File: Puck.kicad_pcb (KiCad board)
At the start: 2 copper layers, 26.6 x 72.5 mm, 19 parts, among them J3 TYPE-C-31-M-12, J4 Conn_01x04_Socket, SW1 SW_Push, SW2 SW_Push, U1 ET6226M, U2 ESP32-C6-MINI-1/U, U4 AP2112K-3.3TRG1, U5 MCP9808T-E_MS

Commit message: feat: Disconnect RX and TX pins
Original-author: Ishan Karmakar <ishan.karmakar24@gmail.com>
Source-commit: 296c2ee0a068d96963a51e7bc8ff53979a0f6f0b
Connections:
- J4 pad 1: /RX -> unconnected-(J4-RX-Pad1)
- J4 pad 3: /TX -> unconnected-(J4-TX-Pad3)
- U2 pad 30: /RX -> unconnected-(U2-U0RXD/GPIO17-Pad30)
- U2 pad 31: /TX -> unconnected-(U2-U0TXD/GPIO16-Pad31)
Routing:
- net /RX: track 13.8 -> 0.00 mm, vias 1 -> 0
- net /TX: track 12.8 -> 0.00 mm, vias 1 -> 0
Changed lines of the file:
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@@
 			(size 0.4 0.8)
 			(layers "F.Cu" "F.Mask" "F.Paste")
-			(net "/RX")
+			(net "unconnected-(U2-U0RXD{slash}GPIO17-Pad30)")
 			(pinfunction "U0RXD/GPIO17_30")
-			(pintype "bidirectional")
+			(pintype "bidirectional+no_connect")
 		)
 		(pad "31" smd rect
@@
 			(size 0.4 0.8)
 			(layers "F.Cu" "F.Mask" "F.Paste")
-			(net "/TX")
+			(net "unconnected-(U2-U0TXD{slash}GPIO16-Pad31)")
 			(pinfunction "U0TXD/GPIO16_31")
-			(pintype "bidirectional")
+			(pintype "bidirectional+no_connect")
 		)
 		(pad "32" smd rect
@@
 			(size 0.7874 0.7874)
 			(layers "B.Cu" "B.Mask")
-			(net "/RX")
+			(net "unconnected-(J4-RX-Pad1)")
 			(pinfunction "RX_1")
-			(pintype "bidirectional")
+			(pintype "bidirectional+no_connect")
 		)
 		(pad "2" connect circle
@@
 			(size 0.7874 0.7874)
 			(layers "B.Cu" "B.Mask")
-			(net "/TX")
+			(net "unconnected-(J4-TX-Pad3)")
 			(pinfunction "TX_3")
-			(pintype "bidirectional")
+			(pintype "bidirectional+no_connect")
 		)
 		(pad "4" connect circle
@@
 		(net "/BOOT")
 	)
-	(segment
-		(start 170.2 130)
-		(end 170 129.8)
-		(width 0.2)
-		(layer "F.Cu")
-		(net "/RX")
-	)
-	(segment
-		(start 171.4 119.6)
-		(end 171.4 119)
-		(width 0.2)
-		(layer "F.Cu")
-		(net "/RX")
-	)
-	(segment
-		(start 170 121)
-		(end 171.4 119.6)
-		(width 0.2)
-		(layer "F.Cu")
-		(net "/RX")
-	)
-	(segment
-		(start 170 129.8)
-		(end 170 121)
-		(width 0.2)
-		(layer "F.Cu")
-		(net "/RX")
-	)
-	(via
-		(at 170.2 130)
-		(size 0.6)
-		(drill 0.3)
-		(layers "F.Cu" "B.Cu")
-		(net "/RX")
-	)
-	(segment
-		(start 171.23 130)
-		(end 170.2 130)
-		(width 0.2)
-		(layer "B.Cu")
-		(net "/RX")
-	)
-	(segment
-		(start 172 129.23)
-		(end 171.23 130)
-		(width 0.2)
-		(layer "B.Cu")
-		(net "/RX")
-	)
-	(segment
-		(start 170.6 121)
-		(end 172.2 119.4)
-		(width 0.2)
-		(layer "F.Cu")
-		(net "/TX")
-	)
-	(segment
-		(start 172.2 119.4)
-		(end 172.2 119)
-		(width 0.2)
-		(layer "F.Cu")
-		(net "/TX")
-	)
-	(segment
-		(start 170.6 129.2)
-		(end 170.6 121)
-		(width 0.2)
-		(layer "F.Cu")
-		(net "/TX")
-	)
-	(via
-		(at 170.6 129.2)
-		(size 0.6)
-		(drill 0.3)
-		(layers "F.Cu" "B.Cu")
-		(net "/TX")
-	)
-	(segment
-		(start 171.84 127.96)
-		(end 170.6 129.2)
-		(width 0.2)
-		(layer "B.Cu")
-		(net "/TX")
-	)
-	(segment
-		(start 172 127.96)
-		(end 171.84 127.96)
-		(width 0.2)
-		(layer "B.Cu")
-		(net "/TX")
-	)
 	(zone

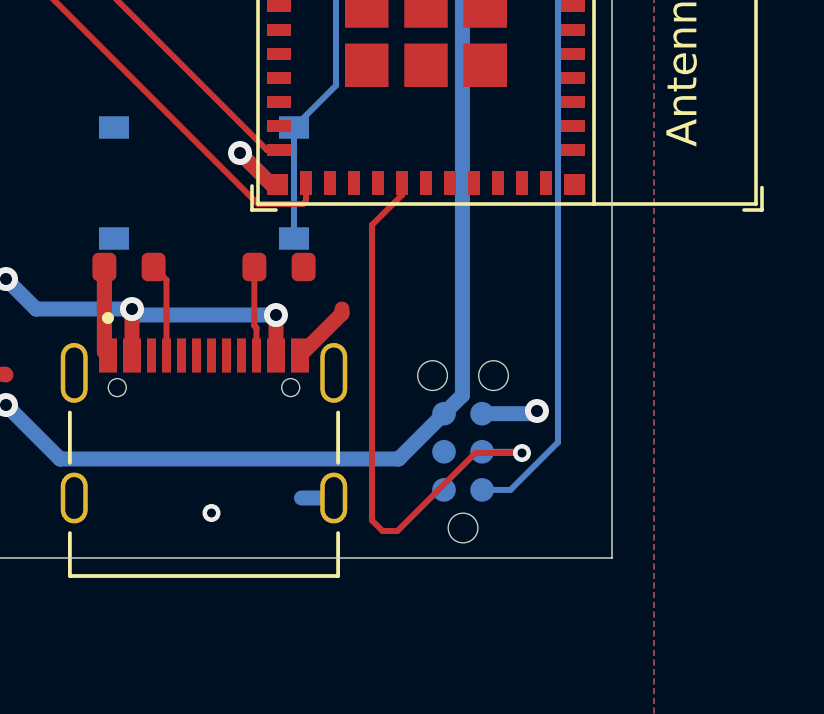
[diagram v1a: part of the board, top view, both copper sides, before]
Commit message: feat: Remove the BOOT pin + NC GPIO9
Original-author: Ishan Karmakar <ishan.karmakar24@gmail.com>
Source-commit: 8bb5acb199ee9e43bb7b500971a5340ad49e3dfa
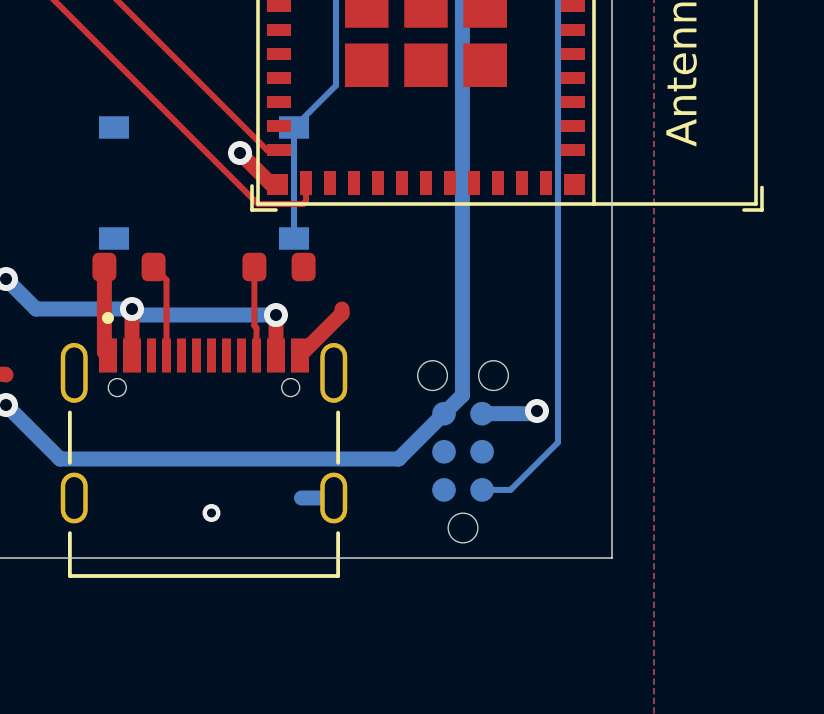
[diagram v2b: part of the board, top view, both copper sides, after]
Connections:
- J4 pad 4: /BOOT -> unconnected-(J4-BOOT-Pad4)
- U2 pad 23: /IO9 -> unconnected-(U2-GPIO9-Pad23)
- U2 pad 29: /BOOT -> unconnected-(U2-GPIO23-Pad29)
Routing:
- net /BOOT: track 19.2 -> 0.00 mm, vias 1 -> 0
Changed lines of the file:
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@@
 			(size 0.4 0.8)
 			(layers "F.Cu" "F.Mask" "F.Paste")
-			(net "/IO9")
+			(net "unconnected-(U2-GPIO9-Pad23)")
 			(pinfunction "GPIO9_23")
-			(pintype "bidirectional")
+			(pintype "bidirectional+no_connect")
 		)
 		(pad "24" smd rect
@@
 			(size 0.4 0.8)
 			(layers "F.Cu" "F.Mask" "F.Paste")
-			(net "/BOOT")
+			(net "unconnected-(U2-GPIO23-Pad29)")
 			(pinfunction "GPIO23_29")
-			(pintype "bidirectional")
+			(pintype "bidirectional+no_connect")
 		)
 		(pad "30" smd rect
@@
 			(size 0.7874 0.7874)
 			(layers "B.Cu" "B.Mask")
-			(net "/BOOT")
+			(net "unconnected-(J4-BOOT-Pad4)")
 			(pinfunction "BOOT_4")
-			(pintype "bidirectional")
+			(pintype "bidirectional+no_connect")
 		)
 		(pad "5" connect circle
@@
 		(net "/IO5")
 	)
-	(segment
-		(start 169.6 130.248529)
-		(end 169.6 120.4)
-		(width 0.2)
-		(layer "F.Cu")
-		(net "/BOOT")
-	)
-	(segment
-		(start 169.951471 130.6)
-		(end 169.6 130.248529)
-		(width 0.2)
-		(layer "F.Cu")
-		(net "/BOOT")
-	)
-	(segment
-		(start 173.048529 128)
-		(end 170.448529 130.6)
-		(width 0.2)
-		(layer "F.Cu")
-		(net "/BOOT")
-	)
-	(segment
-		(start 170.448529 130.6)
-		(end 169.951471 130.6)
-		(width 0.2)
-		(layer "F.Cu")
-		(net "/BOOT")
-	)
-	(segment
-		(start 170.6 119.4)
-		(end 170.6 119)
-		(width 0.2)
-		(layer "F.Cu")
-		(net "/BOOT")
-	)
-	(segment
-		(start 174.6 128)
-		(end 173.048529 128)
-		(width 0.2)
-		(layer "F.Cu")
-		(net "/BOOT")
-	)
-	(segment
-		(start 169.6 120.4)
-		(end 170.6 119.4)
-		(width 0.2)
-		(layer "F.Cu")
-		(net "/BOOT")
-	)
-	(via
-		(at 174.6 128)
-		(size 0.6)
-		(drill 0.3)
-		(layers "F.Cu" "B.Cu")
-		(net "/BOOT")
-	)
-	(segment
-		(start 173.27 127.96)
-		(end 174.56 127.96)
-		(width 0.2)
-		(layer "B.Cu")
-		(net "/BOOT")
-	)
-	(segment
-		(start 174.56 127.96)
-		(end 174.6 128)
-		(width 0.2)
-		(layer "B.Cu")
-		(net "/BOOT")
-	)
 	(zone

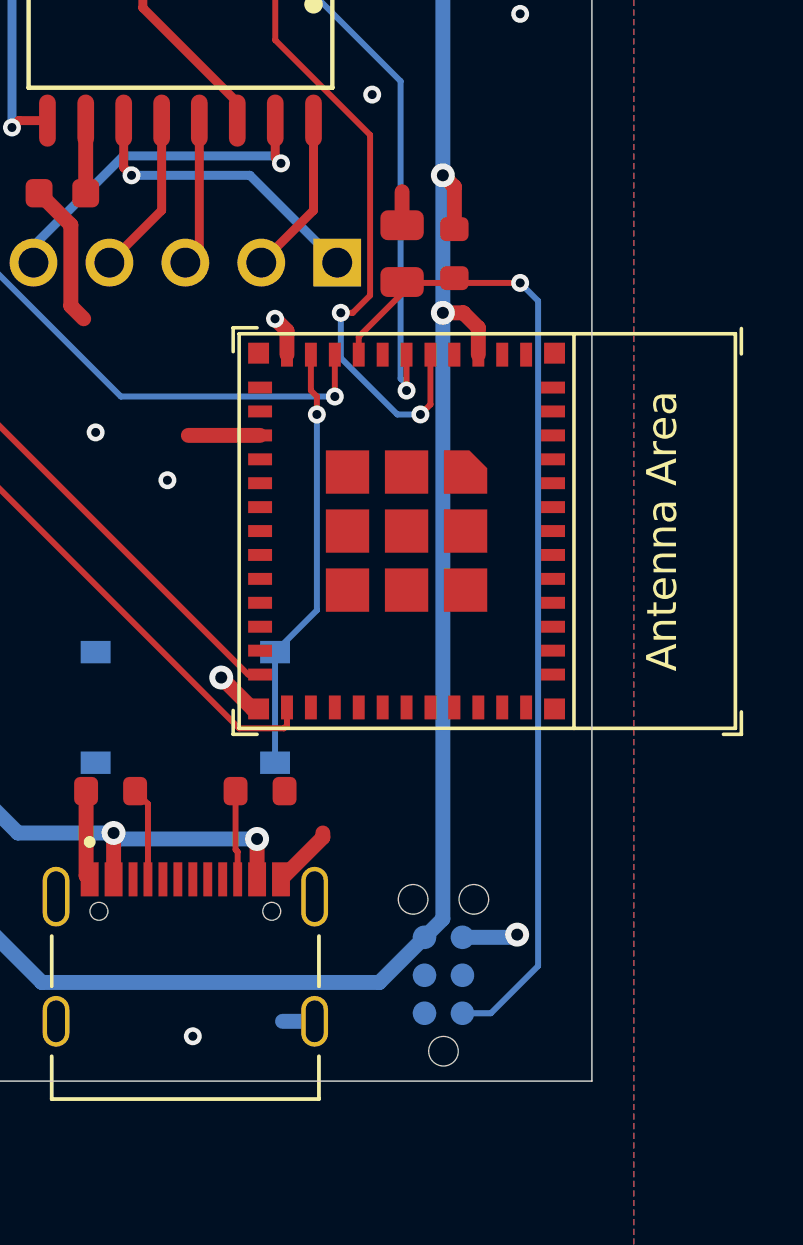
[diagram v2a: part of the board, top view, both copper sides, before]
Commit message: feat: Remove autoprogramming sheet
Original-author: Ishan Karmakar <ishan.karmakar24@gmail.com>
Source-commit: 11d90a359a53dbe271e216bf89b8d8400085b4c9
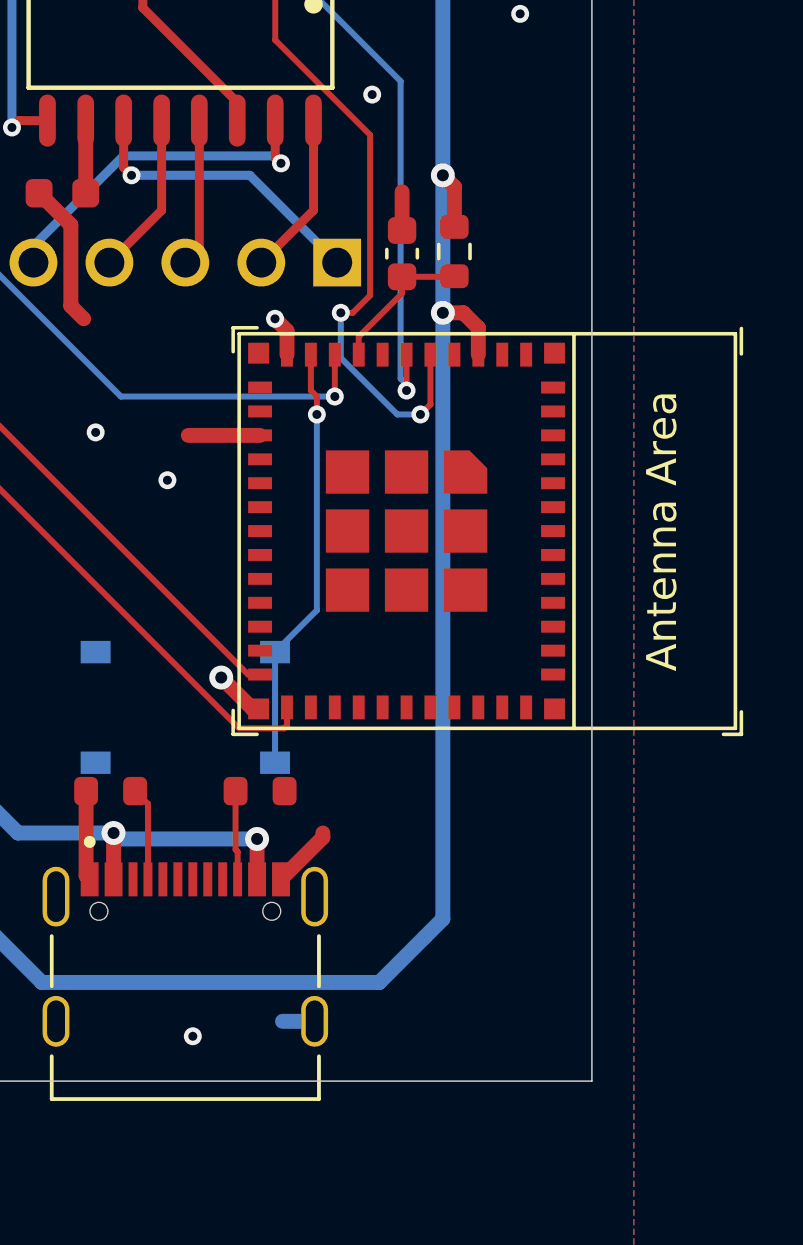
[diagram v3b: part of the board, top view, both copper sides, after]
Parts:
- removed C6: 100nF, PCM_JLCPCB:C_0805
- removed J4: Conn_01x04_Socket, Connector:Tag-Connect_TC2030-IDC-NL_2x03_P1.27mm_Vertical
- removed R7: 10kΩ, PCM_JLCPCB:R_0603
- added C2: 1uF, Capacitor_SMD:C_0603_1608Metric, F.Cu at (171.2, 103.8)
- added R1: 10k, Resistor_SMD:R_0603_1608Metric, F.Cu at (173.0, 103.8)
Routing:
- net /EN: track 33.0 -> 4.96 mm, vias 1 -> 0
- net GND: track 34.6 -> 32.9 mm, vias 16 -> 15

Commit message: feat: Wire D+ and D- from Type C recepticle to ESP32 pins
Original-author: Ishan Karmakar <ishan.karmakar24@gmail.com>
Source-commit: f485fb4ecb58e7db9c11b8a83e3a2328aeb9ad39
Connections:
- J3 pad A6: unconnected-(J3-DP1-PadA6) -> /D+
- J3 pad A7: unconnected-(J3-DN1-PadA7) -> /D-
- J3 pad B6: unconnected-(J3-DP2-PadB6) -> /D+
- J3 pad B7: unconnected-(J3-DN2-PadB7) -> /D-
- U2 pad 17: unconnected-(U2-GPIO12/USB_D--Pad17) -> /D-
- U2 pad 18: unconnected-(U2-GPIO13/USB_D+-Pad18) -> /D+
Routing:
- net /D-: track 0.00 -> 16.8 mm, vias 0 -> 2
- net /D+: track 0.00 -> 15.4 mm, vias 0 -> 2
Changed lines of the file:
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@@
 			)
 		)
-		(sheetname "/Type C Recepticle (No Flash)/")
+		(sheetname "/Type C Recepticle/")
 		(sheetfile "Type C Recepticle.kicad_sch")
 		(units
@@
 			(size 0.3 1.14)
 			(layers "F.Cu" "F.Paste")
-			(net "unconnected-(J3-DP1-PadA6)")
+			(net "/D+")
 			(pinfunction "DP1_A6")
-			(pintype "bidirectional+no_connect")
+			(pintype "bidirectional")
 		)
 		(pad "A7" smd rect
@@
 			(size 0.3 1.14)
 			(layers "F.Cu" "F.Paste")
-			(net "unconnected-(J3-DN1-PadA7)")
+			(net "/D-")
 			(pinfunction "DN1_A7")
-			(pintype "bidirectional+no_connect")
+			(pintype "bidirectional")
 		)
 		(pad "A8" smd rect
@@
 			(size 0.3 1.14)
 			(layers "F.Cu" "F.Paste")
-			(net "unconnected-(J3-DP2-PadB6)")
+			(net "/D+")
 			(pinfunction "DP2_B6")
-			(pintype "bidirectional+no_connect")
+			(pintype "bidirectional")
 		)
 		(pad "B7" smd rect
@@
 			(size 0.3 1.14)
 			(layers "F.Cu" "F.Paste")
-			(net "unconnected-(J3-DN2-PadB7)")
+			(net "/D-")
 			(pinfunction "DN2_B7")
-			(pintype "bidirectional+no_connect")
+			(pintype "bidirectional")
 		)
 		(pad "B8" smd rect
@@
 		)
 		(property ki_fp_filters "R_*")
-		(sheetname "/Type C Recepticle (No Flash)/")
+		(sheetname "/Type C Recepticle/")
 		(sheetfile "Type C Recepticle.kicad_sch")
 		(units
@@
 		)
 		(property ki_fp_filters "R_*")
-		(sheetname "/Type C Recepticle (No Flash)/")
+		(sheetname "/Type C Recepticle/")
 		(sheetfile "Type C Recepticle.kicad_sch")
 		(units
@@
 			(size 0.4 0.8)
 			(layers "F.Cu" "F.Mask" "F.Paste")
-			(net "unconnected-(U2-GPIO12{slash}USB_D--Pad17)")
+			(net "/D-")
 			(pinfunction "GPIO12/USB_D-_17")
-			(pintype "bidirectional+no_connect")
+			(pintype "bidirectional")
 		)
 		(pad "18" smd rect
@@
 			(size 0.4 0.8)
 			(layers "F.Cu" "F.Mask" "F.Paste")
-			(net "unconnected-(U2-GPIO13{slash}USB_D+-Pad18)")
+			(net "/D+")
 			(pinfunction "GPIO13/USB_D+_18")
-			(pintype "bidirectional+no_connect")
+			(pintype "bidirectional")
 		)
 		(pad "19" smd rect
@@
 	)
 	(segment
+		(start 171.25 104.595)
+		(end 172.98 104.595)
+		(width 0.2)
+		(layer "F.Cu")
+		(net "/EN")
+	)
+	(segment
+		(start 169.8 107.2)
+		(end 169.8 106.6)
+		(width 0.2)
+		(layer "F.Cu")
+		(net "/EN")
+	)
+	(segment
+		(start 172.98 104.595)
+		(end 173 104.575)
+		(width 0.2)
+		(layer "F.Cu")
+		(net "/EN")
+	)
+	(segment
+		(start 169.8 106.6)
+		(end 171.25 105.15)
+		(width 0.2)
+		(layer "F.Cu")
+		(net "/EN")
+	)
+	(segment
+		(start 171.25 105.15)
+		(end 171.25 104.595)
+		(width 0.2)
+		(layer "F.Cu")
+		(net "/EN")
+	)
+	(segment
 		(start 168.2875 93.1675)
 		(end 168.2875 93.63)
@@
 	)
 	(segment
-		(start 171.25 104.595)
-		(end 172.98 104.595)
-		(width 0.2)
-		(layer "F.Cu")
-		(net "/EN")
-	)
-	(segment
-		(start 169.8 107.2)
-		(end 169.8 106.6)
-		(width 0.2)
-		(layer "F.Cu")
-		(net "/EN")
-	)
-	(segment
-		(start 172.98 104.595)
-		(end 173 104.575)
-		(width 0.2)
-		(layer "F.Cu")
-		(net "/EN")
-	)
-	(segment
-		(start 169.8 106.6)
-		(end 171.25 105.15)
-		(width 0.2)
-		(layer "F.Cu")
-		(net "/EN")
-	)
-	(segment
-		(start 171.25 105.15)
-		(end 171.25 104.595)
-		(width 0.2)
-		(layer "F.Cu")
-		(net "/EN")
-	)
-	(segment
 		(start 169 108.6)
 		(end 169 107.2)
@@
 		(net "/IO5")
 	)
+	(segment
+		(start 163.75 123.1364)
+		(end 163.75 124.75)
+		(width 0.2)
+		(layer "F.Cu")
+		(net "/D+")
+	)
+	(segment
+		(start 164.75 124.75)
+		(end 164.75 123.1636)
+		(width 0.2)
+		(layer "F.Cu")
+		(net "/D+")
+	)
+	(segment
+		(start 164.2364 122.65)
+		(end 163.75 123.1364)
+		(width 0.2)
+		(layer "F.Cu")
+		(net "/D+")
+	)
+	(segment
+		(start 164.833865 114.216935)
+		(end 164.833865 115.785335)
+		(width 0.2)
+		(layer "F.Cu")
+		(net "/D+")
+	)
+	(segment
+		(start 164.75 123.1636)
+		(end 164.2364 122.65)
+		(width 0.2)
+		(layer "F.Cu")
+		(net "/D+")
+	)
+	(segment
+		(start 165.9508 113.1)
+		(end 164.833865 114.216935)
+		(width 0.2)
+		(layer "F.Cu")
+		(net "/D+")
+	)
+	(segment
+		(start 166.5 113.1)
+		(end 165.9508 113.1)
+		(width 0.2)
+		(layer "F.Cu")
+		(net "/D+")
+	)
+	(via
+		(at 164.833865 115.785335)
+		(size 0.6)
+		(drill 0.3)
+		(layers "F.Cu" "B.Cu")
+		(net "/D+")
+	)
+	(via
+		(at 164.2364 122.65)
+		(size 0.6)
+		(drill 0.3)
+		(layers "F.Cu" "B.Cu")
+		(net "/D+")
+	)
+	(segment
+		(start 164.833865 115.785335)
+		(end 164.2364 116.3828)
+		(width 0.2)
+		(layer "B.Cu")
+		(net "/D+")
+	)
+	(segment
+		(start 164.2364 116.3828)
+		(end 164.2364 122.65)
+		(width 0.2)
+		(layer "B.Cu")
+		(net "/D+")
+	)
+	(segment
+		(start 166.5 112.3)
+		(end 165.9 112.3)
+		(width 0.2)
+		(layer "F.Cu")
+		(net "/D-")
+	)
+	(segment
+		(start 164.233865 113.966135)
+		(end 164.233865 115.185338)
+		(width 0.2)
+		(layer "F.Cu")
+		(net "/D-")
+	)
+	(segment
+		(start 163.25 125.57)
+		(end 163.3 125.62)
+		(width 0.2)
+		(layer "F.Cu")
+		(net "/D-")
+	)
+	(segment
+		(start 163.25 122.75)
+		(end 163.25 124.75)
+		(width 0.2)
+		(layer "F.Cu")
+		(net "/D-")
+	)
+	(segment
+		(start 164.25 125.57)
+		(end 164.25 124.75)
+		(width 0.2)
+		(layer "F.Cu")
+		(net "/D-")
+	)
+	(segment
+		(start 165.9 112.3)
+		(end 164.233865 113.966135)
+		(width 0.2)
+		(layer "F.Cu")
+		(net "/D-")
+	)
+	(segment
+		(start 163.3 125.62)
+		(end 164.2 125.62)
+		(width 0.2)
+		(layer "F.Cu")
+		(net "/D-")
+	)
+	(segment
+		(start 163.35 122.65)
+		(end 163.25 122.75)
+		(width 0.2)
+		(layer "F.Cu")
+		(net "/D-")
+	)
+	(segment
+		(start 164.2 125.62)
+		(end 164.25 125.57)
+		(width 0.2)
+		(layer "F.Cu")
+		(net "/D-")
+	)
+	(segment
+		(start 163.25 124.75)
+		(end 163.25 125.57)
+		(width 0.2)
+		(layer "F.Cu")
+		(net "/D-")
+	)
+	(via
+		(at 164.233865 115.185338)
+		(size 0.6)
+		(drill 0.3)
+		(layers "F.Cu" "B.Cu")
+		(net "/D-")
+	)
+	(via
+		(at 163.35 122.65)
+		(size 0.6)
+		(drill 0.3)
+		(layers "F.Cu" "B.Cu")
+		(net "/D-")
+	)
+	(segment
+		(start 164.233865 115.185338)
+		(end 163.35 116.069203)
+		(width 0.2)
+		(layer "B.Cu")
+		(net "/D-")
+	)
+	(segment
+		(start 163.35 116.069203)
+		(end 163.35 122.65)
+		(width 0.2)
+		(layer "B.Cu")
+		(net "/D-")
+	)
 	(zone
